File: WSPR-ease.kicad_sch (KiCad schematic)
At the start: 34 parts, among them J101 GNSS Ant, J102 Tx Ant, J103 USB_C_16P_Stacked, Q101 MMBF170, U101 ATGM336H-5N31, U102 ESP32-S3-WROOM-1-N8R8, U103 NCP1117-3.3_SOT223, U104 SRV05-4

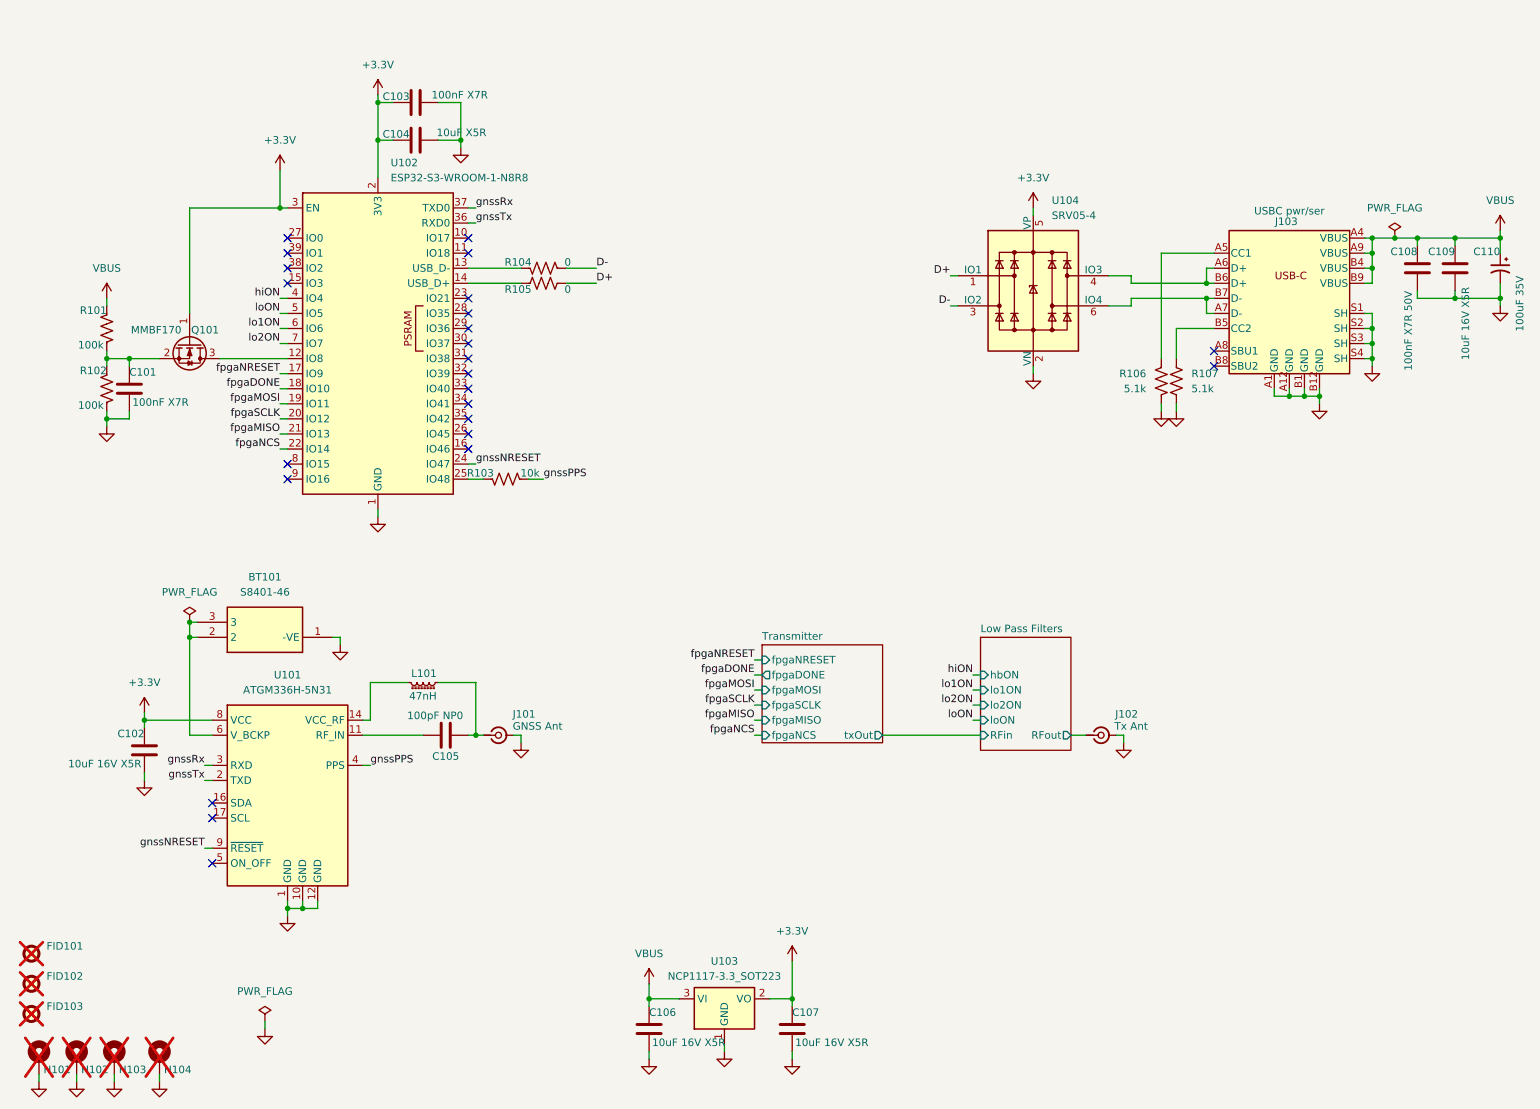
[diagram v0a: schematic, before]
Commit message: Tarted up, 3d models applied, better footprints and BOM, ready to submit for PCBA
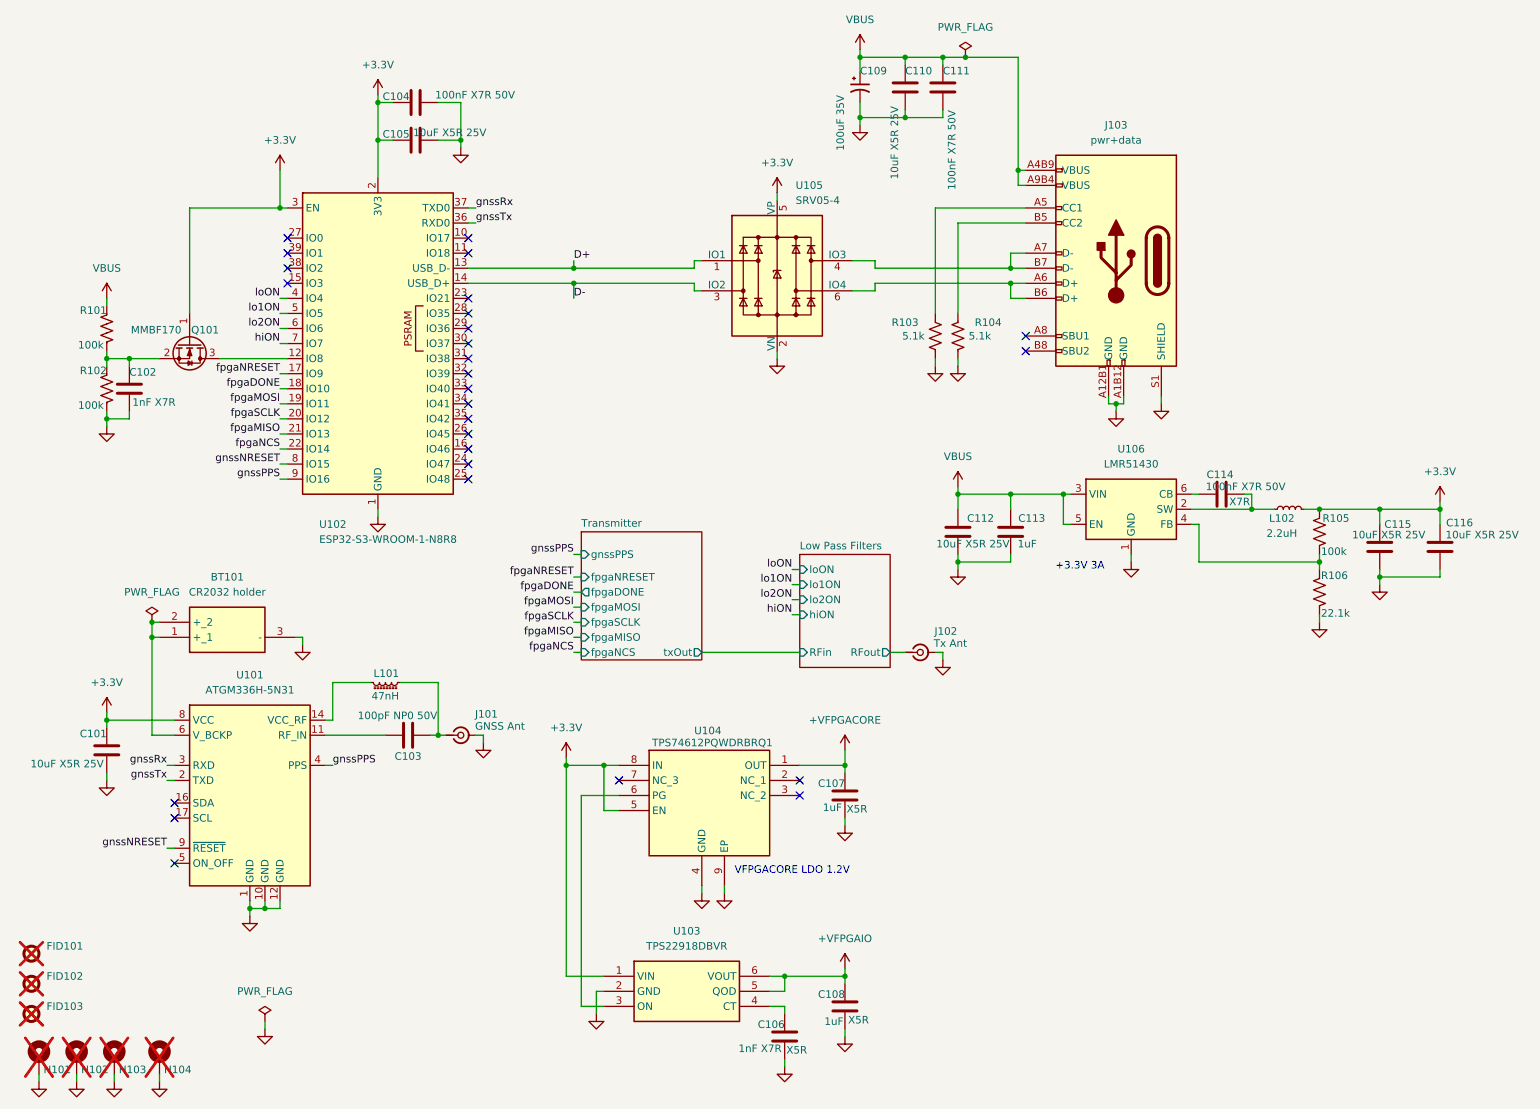
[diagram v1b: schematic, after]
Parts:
- removed J103: USB_C_16P_Stacked, Connector_USB:USB_C_Receptacle_HRO_TYPE-C-31-M-12, symbol Library:USB_C_Receptacle_HRO_16P_Stacked
- removed R107: 5.1k, Resistor_SMD:R_0603_1608Metric, symbol Device:R_US
- removed U103: NCP1117-3.3_SOT223, Package_TO_SOT_SMD:SOT-223-3_TabPin2, symbol Regulator_Linear:NCP1117-3.3_SOT223
- added C108, C113: 1uF, Capacitor_SMD:C_0402_1005Metric, symbol Device:C
- added C112, C115, C116: 10uF X5R 25V, Capacitor_SMD:C_0603_1608Metric, symbol Device:C
- added C114: 100nF X7R 50V, Capacitor_SMD:C_0603_1608Metric, symbol Device:C
- added J103: pwr+data, Library:USB_C_Receptacle_HRO_TYPE-C-31-M-12-bursted, symbol Library:USB_C_Receptacle_USB2.0_16P-bursted
- added L102: 2.2uH, Inductor_SMD:L_0805_2012Metric, symbol Device:L_Small
- added U103: TPS22918DBVR, Package_TO_SOT_SMD:SOT-23-6, symbol Library:TPS22918DBVR
- added U104: TPS74612PQWDRBRQ1, SON65P300X300X100-9N-D, symbol Library:TPS74612PQWDRBRQ1
- added U106: LMR51430, Package_TO_SOT_SMD:SOT-23-6, symbol Regulator_Switching:LMR51430
- BT101: value S8401-46 -> CR2032 holder; footprint Library:S8401-46 -> BATHLD014THM; symbol Library:S8401-46 -> Library:BAT-HLD-014-THM; Height (none) -> 6; LCSC C5904513 -> C31226699; Manufacturer_Name Harwin -> TE Connectivity; Manufacturer_Part_Number S8401-46 -> BAT-HLD-014-THM; Mouser Part Number 855-S8401-46 -> 712-BAT-HLD-014-THM; Mouser Price/Stock https://www.mouser.co.uk/ProductDetail/Harwin/S8401-46?qs=Q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 -> https://www.mouser.co.uk/ProductDetail/Linx-Technologies/BA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
- C101: renamed from C102; value 10uF 16V X5R -> 10uF X5R 25V; footprint Capacitor_SMD:C_0805_2012Metric -> Capacitor_SMD:C_0603_1608Metric; LCSC C1713 -> C96446
- C102: renamed from C101; value 100nF X7R -> 1nF X7R; footprint Capacitor_SMD:C_0603_1608Metric -> Capacitor_SMD:C_0402_1005Metric; LCSC C14663 -> C106205
- C103: renamed from C105; value 100pF NP0 -> 100pF NP0 50V; footprint Capacitor_SMD:C_0603_1608Metric -> Capacitor_SMD:C_0402_1005Metric; LCSC C14665 -> C106200
- C104: renamed from C103; value 100nF X7R -> 100nF X7R 50V; LCSC C14663 -> C24452
- C105: renamed from C104; value 10uF X5R -> 10uF X5R 25V; LCSC C19702 -> C96446
- C106: value 10uF 16V X5R -> 1nF X7R; footprint Capacitor_SMD:C_0805_2012Metric -> Capacitor_SMD:C_0402_1005Metric; LCSC C1713 -> C106205; LCSC_PN (none) -> C301928; Manufacturer (none) -> Murata; Mouser_PN (none) -> 81-GRM155R61E105KE1D; cap-type (none) -> X5R; working-voltage (none) -> 25V
- C107: value 10uF 16V X5R -> 1uF; footprint Capacitor_SMD:C_0805_2012Metric -> Capacitor_SMD:C_0402_1005Metric; LCSC C1713 -> C14445; LCSC_PN (none) -> C301928; Manufacturer (none) -> Murata; Mouser_PN (none) -> 81-GRM155R61E105KE1D; cap-type (none) -> X5R; working-voltage (none) -> 25V
- C109: renamed from C110; footprint Capacitor_SMD:CP_Elec_8x10.5 -> Library:CAPAE850X1050N
- C110: renamed from C109; value 10uF 16V X5R -> 10uF X5R 25V; footprint Capacitor_SMD:C_0805_2012Metric -> Capacitor_SMD:C_0603_1608Metric; LCSC C1713 -> C96446
- C111: renamed from C108; LCSC C14663 -> C24452
- R101, R102: footprint Resistor_SMD:R_0603_1608Metric -> Resistor_SMD:R_0402_1005Metric; LCSC C7311067 -> C60491
- R103: value 10k -> 5.1k; footprint Resistor_SMD:R_0603_1608Metric -> Resistor_SMD:R_0402_1005Metric; LCSC C2930027 -> C105872; LCSC_PN (none) -> C854378
- R104: value 0 -> 5.1k; LCSC C2930027 -> C105872; LCSC_PN (none) -> C854378
- R105: value 0 -> 100k; LCSC C2930027 -> C60491; LCSC_PN (none) -> C728576
- R106: value 5.1k -> 22.1k; footprint Resistor_SMD:R_0603_1608Metric -> Resistor_SMD:R_0402_1005Metric; LCSC C2907114 -> C82868; LCSC_PN (none) -> C284424
- renumbered U104 to U105
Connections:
- net +3.3V: now also R105.2, C115.1, C116.1, L102.2, U103.1 (VIN), U104.5 (EN), U104.8 (IN); no longer C107.1
- net D+: now also U102.13 (USB_D-); no longer R105.2
- net D-: now also U102.14 (USB_D+); no longer R104.2
- net GND: now also BT101.3 (-), R103.2, R104.2, R106.1, C108.2, C112.2, C113.2, C115.2, C116.2, J103.A12B1 (GND), J103.A1B12 (GND), J103.S1 (SHIELD), U103.2 (GND), U104.4 (GND), U104.9 (EP), U106.1 (GND); no longer BT101.1 (-VE), R106.2
- net VBUS: now also C112.1, C113.1, J103.A4B9 (VBUS), J103.A9B4 (VBUS), U106.3 (VIN), U106.5 (EN); no longer C106.1
- net gnssNRESET: now also U102.8 (IO15); no longer U102.24 (IO47)
- net gnssPPS: now also U102.9 (IO16); no longer R103.2
- net hiON: now also U102.7 (IO7); no longer U102.4 (IO4)
- net lo1ON: now also U102.5 (IO5); no longer U102.6 (IO6)
- net lo2ON: now also U102.6 (IO6); no longer U102.7 (IO7)
- net loON: now also U102.4 (IO4); no longer U102.5 (IO5)
- net at R104.1: now also J103.B5 (CC2); no longer U102.13 (USB_D-)
- net at BT101.2 (+_2), U101.6 (V_BCKP): now also BT101.1 (+_1); no longer BT101.3
- net at U105.4 (IO3): now also J103.A7 (D-), J103.B7 (D-)
- net at U105.6 (IO4): now also J103.A6 (D+), J103.B6 (D+)
- net at R105.1: now also R106.2, U106.4 (FB); no longer U102.14 (USB_D+)
- net at R103.1: now also J103.A5 (CC1); no longer U102.25 (IO48)
- new net: C114.2, L102.1, U106.2 (SW)
- new net: C114.1, U106.6 (CB)
- new net: U103.3 (ON), U104.6 (PG)
- new net: C106.1, U103.4 (CT)
- new net +VFPGACORE: C107.1, U104.1 (OUT)
- new net +VFPGAIO: C108.1, U103.5 (QOD), U103.6 (VOUT)
- no-connect marks 24 -> 27
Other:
- sheet Low Pass Filters ports: added hiON; removed hbON
- sheet Transmitter ports: added gnssPPS; removed none
- note added: "+3.3V 3A"
- note added: "VFPGACORE LDO 1.2V"
- moved on the sheet: BT101, C101, C103, C109, C110, C111, J101, J102, L101, U101, U105

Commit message: Small changes to part numbers to ease supply chain issues for build
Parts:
- BT101: LCSC C31226699 -> C6750449
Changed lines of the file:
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@@
 			)
 		)
-		(property "LCSC" "C31226699"
+		(property "LCSC" "C6750449"
 			(at 36.83 125.73 90)
 			(effects
